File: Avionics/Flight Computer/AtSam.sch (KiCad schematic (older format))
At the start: 0 parts

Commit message: Restarted initial layout and cleaned up decoupling/RF layout.
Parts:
- added U12: ATSAME70Q21A-AN, Housings_QFP:LQFP-144_20x20mm_Pitch0.5mm, symbol ATSAME70Q21A-AN
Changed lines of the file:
@@
 EESchema Schematic File Version 2
+LIBS:Flight Computer-rescue
 LIBS:device
 LIBS:rfcom
@@
 $Descr A4 11693 8268
 encoding utf-8
-Sheet 2 7
+Sheet 2 9
 Title ""
 Date ""
@@
 Comment4 ""
 $EndDescr
+$Comp
+L ATSAME70Q21A-AN U12
+U 1 1 58B40577
+P 3150 1900
+F 0 "U12" H 3150 3067 50  0000 C CNN
+F 1 "ATSAME70Q21A-AN" H 3150 2976 50  0000 C CNN
+F 2 "Housings_QFP:LQFP-144_20x20mm_Pitch0.5mm" H 800 4750 50  0001 C CIN
+F 3 "http://www.atmel.com/Images/Atmel-11296-32-bit-Cortex-M7-Microcontroller-SAM-E70Q-SAM-E70N-SAM-E70J_Datasheet.pdf" H 800 -4300 50  0001 C CNN
+	1    3150 1900
+	1    0    0    -1
+$EndComp
+$Comp
+L ATSAME70Q21A-AN U12
+U 2 1 58B4060F
+P 3150 4050
+F 0 "U12" H 3150 5067 50  0000 C CNN
+F 1 "ATSAME70Q21A-AN" H 3150 4976 50  0000 C CNN
+F 2 "Housings_QFP:LQFP-144_20x20mm_Pitch0.5mm" H -100 3900 50  0001 C CIN
+F 3 "http://www.atmel.com/Images/Atmel-11296-32-bit-Cortex-M7-Microcontroller-SAM-E70Q-SAM-E70N-SAM-E70J_Datasheet.pdf" H -100 -5150 50  0001 C CNN
+	2    3150 4050
+	1    0    0    -1
+$EndComp
+$Comp
+L ATSAME70Q21A-AN U12
+U 3 1 58B4068D
+P 2900 5950
+F 0 "U12" H 2800 6750 50  0000 L CNN
+F 1 "ATSAME70Q21A-AN" H 2500 6650 50  0000 L CNN
+F 2 "Housings_QFP:LQFP-144_20x20mm_Pitch0.5mm" H -4500 8350 50  0001 C CIN
+F 3 "http://www.atmel.com/Images/Atmel-11296-32-bit-Cortex-M7-Microcontroller-SAM-E70Q-SAM-E70N-SAM-E70J_Datasheet.pdf" H -4500 -700 50  0001 C CNN
+	3    2900 5950
+	1    0    0    -1
+$EndComp
+$Comp
+L ATSAME70Q21A-AN U12
+U 4 1 58B406DD
+P 7250 1750
+F 0 "U12" H 7250 2767 50  0000 C CNN
+F 1 "ATSAME70Q21A-AN" H 7250 2676 50  0000 C CNN
+F 2 "Housings_QFP:LQFP-144_20x20mm_Pitch0.5mm" H -50 2100 50  0001 C CIN
+F 3 "http://www.atmel.com/Images/Atmel-11296-32-bit-Cortex-M7-Microcontroller-SAM-E70Q-SAM-E70N-SAM-E70J_Datasheet.pdf" H -50 -6950 50  0001 C CNN
+	4    7250 1750
+	1    0    0    -1
+$EndComp
+$Comp
+L ATSAME70Q21A-AN U12
+U 5 1 58B4072D
+P 7250 3850
+F 0 "U12" H 7250 4867 50  0000 C CNN
+F 1 "ATSAME70Q21A-AN" H 7250 4776 50  0000 C CNN
+F 2 "Housings_QFP:LQFP-144_20x20mm_Pitch0.5mm" H -2400 6150 50  0001 C CIN
+F 3 "http://www.atmel.com/Images/Atmel-11296-32-bit-Cortex-M7-Microcontroller-SAM-E70Q-SAM-E70N-SAM-E70J_Datasheet.pdf" H -2400 -2900 50  0001 C CNN
+	5    7250 3850
+	1    0    0    -1
+$EndComp
+$Comp
+L ATSAME70Q21A-AN U12
+U 6 1 58B407D7
+P 7000 5450
+F 0 "U12" H 6900 5950 50  0000 L CNN
+F 1 "ATSAME70Q21A-AN" H 6600 5850 50  0000 L CNN
+F 2 "Housings_QFP:LQFP-144_20x20mm_Pitch0.5mm" H -2500 5250 50  0001 C CIN
+F 3 "http://www.atmel.com/Images/Atmel-11296-32-bit-Cortex-M7-Microcontroller-SAM-E70Q-SAM-E70N-SAM-E70J_Datasheet.pdf" H -2500 -3800 50  0001 C CNN
+	6    7000 5450
+	1    0    0    -1
+$EndComp
 $EndSCHEMATC

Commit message: Nearly completed initial placement.
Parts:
- added C57, C69, C72, C73, C74, C75, C76, C77, C78, C79, C80, C81, C82, C83, C84: 0.1u, Capacitors_SMD:C_0402, symbol C
- added C60, C62, C63, C64, C65: 12p, Capacitors_SMD:C_0402, symbol C
- added C61, C68: 1u, Capacitors_SMD:C_0603, symbol C
- added C85, C86: 4.7u, Capacitors_SMD:C_0603, symbol C
- added L19, L20: MMZ1005Y471CTD25, Inductors_SMD:L_0402, symbol L
- added L21: LQM21FN100M70L, Inductors_SMD:L_0805, symbol L
- added R20: 5.62k, Resistors_SMD:R_0402, symbol R
- added R21: 22k, Resistors_SMD:R_0402, symbol R
- added R22: 15k, Resistors_SMD:R_0402, symbol R
- added R23: 2.2, Resistors_SMD:R_0402, symbol R
- added Y1: 9HT11-32.768KDZB-T, Crystals:Crystal_SMD_2012-2pin_2.0x1.2mm, symbol Crystal
- added Y2: 7V-16.000MAHJ-T, Crystals:Crystal_SMD_3225-4pin_3.2x2.5mm, symbol Crystal_GND24
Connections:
- net labels added: +3.3V, GND, QCS, QIO0, QIO1, QIO2, QIO3, QIO[0..3], QSCK, USBD_N, USBD_P, VBUS_DETECT, VDDPLLUSB, VUSB
- wire segments 0 -> 70
- no-connect marks 0 -> 2
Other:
- note added: "Pin 5"
- note added: "Place one near each VDDCORE pin"
- note added: "Place one near each VDDIO pin"
- moved on the sheet: U12A, U12B, U12C, U12D, U12E, U12F

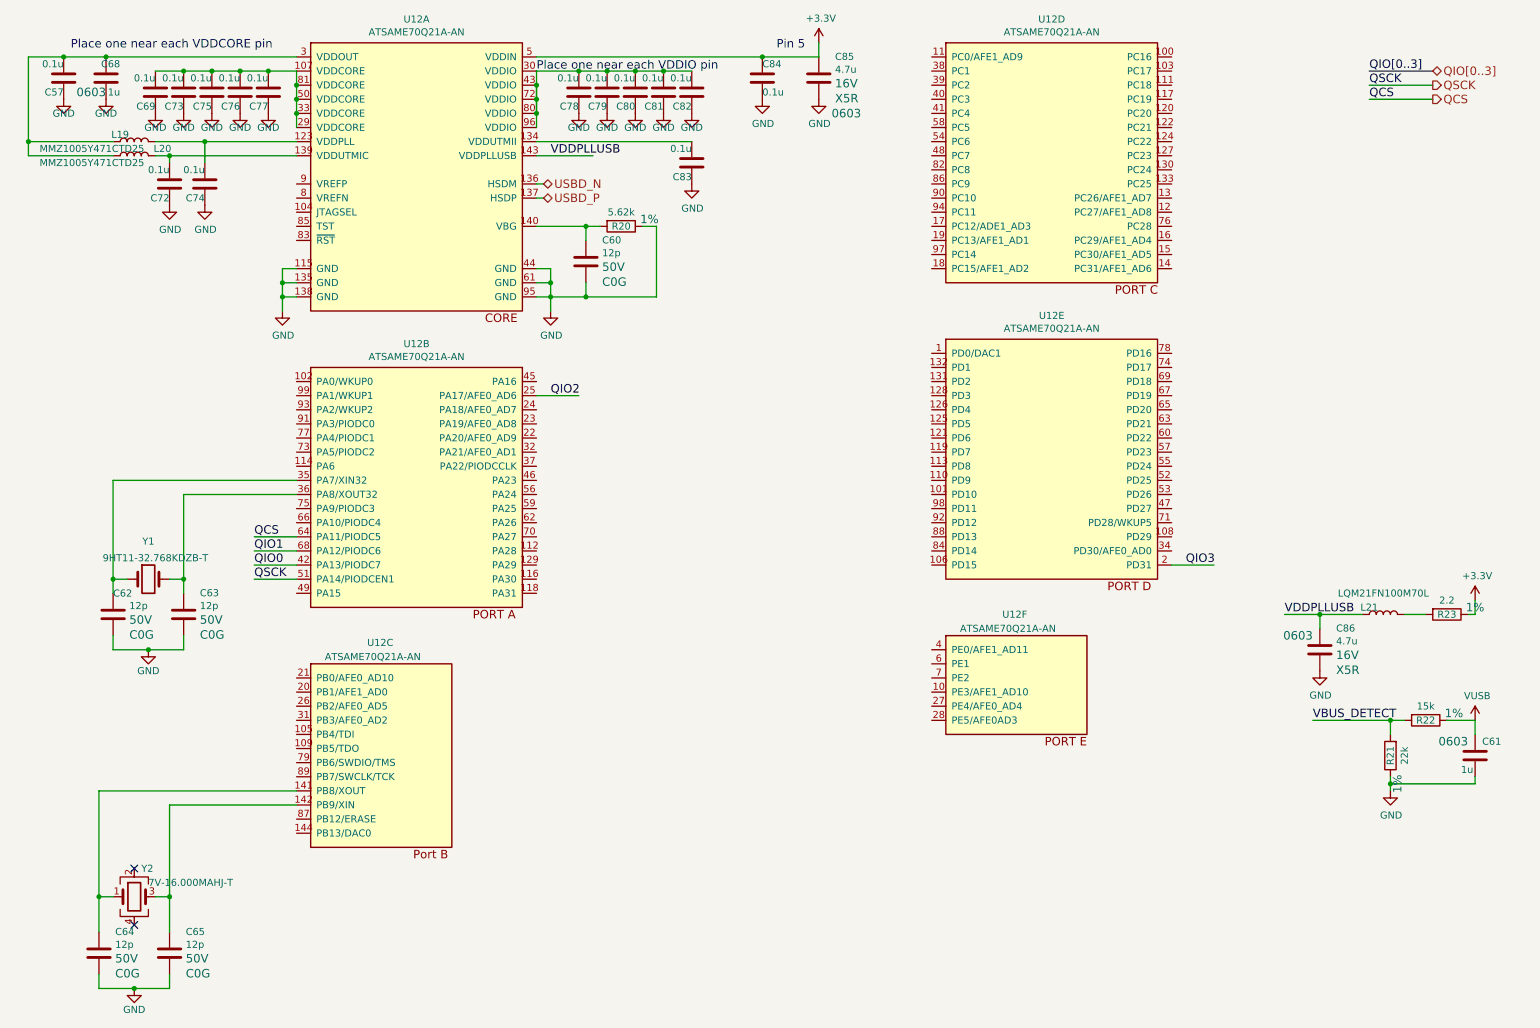
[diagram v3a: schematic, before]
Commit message: Added additional pinout
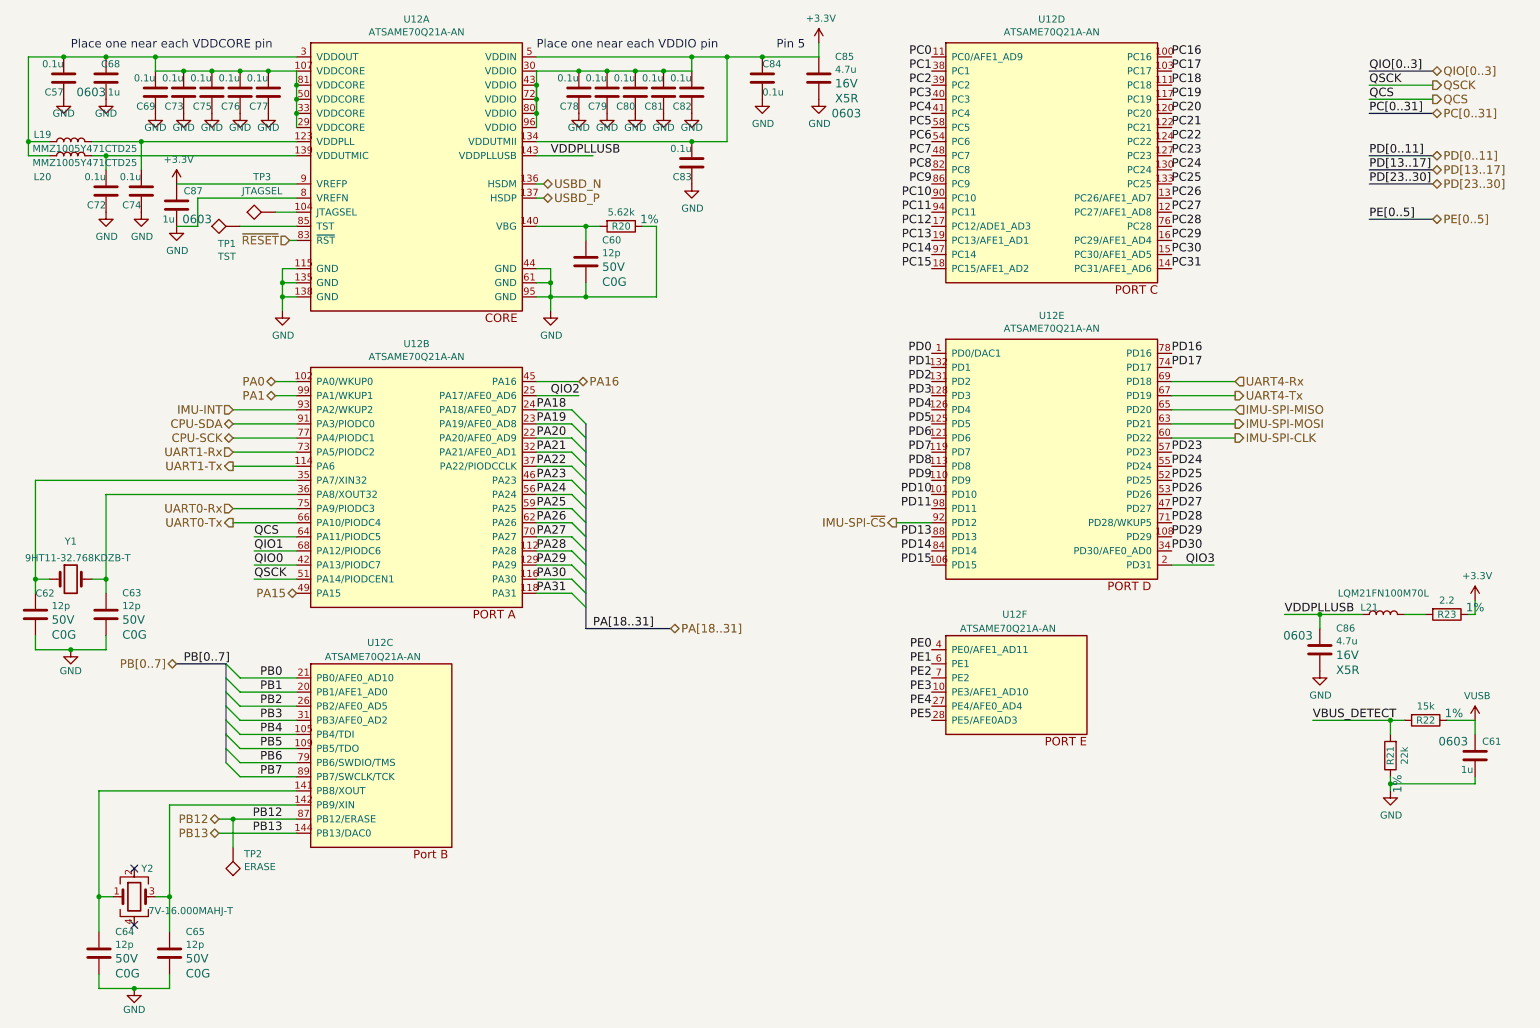
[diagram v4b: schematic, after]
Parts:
- added C87: 1u, Capacitors_SMD:C_0603, symbol C
- added TP1: TST, Measurement_Points:Measurement_Point_Round-SMD-Pad_Small, symbol TEST
- added TP2: ERASE, Measurement_Points:Measurement_Point_Round-SMD-Pad_Small, symbol TEST
- added TP3: JTAGSEL, Measurement_Points:Measurement_Point_Round-SMD-Pad_Small, symbol TEST
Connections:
- net labels added: CPU-SCK, CPU-SDA, IMU-INT, IMU-SPI-CLK, IMU-SPI-MISO, IMU-SPI-MOSI, IMU-SPI-~CS, PA0, PA1, PA15, PA16, PA18, PA19, PA20, PA21, PA22, PA23, PA24, PA25, PA26, PA27, PA28, PA29, PA30, PA31, PA[18..31], PB0, PB1, PB12, PB13, PB2, PB3, PB4, PB5, PB6, PB7, PB[0..7], PC0, PC1, PC10, PC11, PC12, PC13, PC14, PC15, PC16, PC17, PC18, PC19, PC2, PC20, PC21, PC22, PC23, PC24, PC25, PC26, PC27, PC28, PC29, PC3, PC30, PC31, PC4, PC5, PC6, PC7, PC8, PC9, PC[0..31], PD0, PD1, PD10, PD11, PD13, PD14, PD15, PD16, PD17, PD2, PD23, PD24, PD25, PD26, PD27, PD28, PD29, PD3, PD30, PD4, PD5, PD6, PD7, PD8, PD9, PD[0..11], PD[13..17], PD[23..30], PE0, PE1, PE2, PE3, PE4, PE5, PE[0..5], UART0-Rx, UART0-Tx, UART1-Rx, UART1-Tx, UART4-Rx, UART4-Tx, ~RESET
- wire segments 70 -> 121
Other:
- moved on the sheet: C62, C63, C72, C74, L19, L20, Y1

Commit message: Wired up everything and started rearranging layout
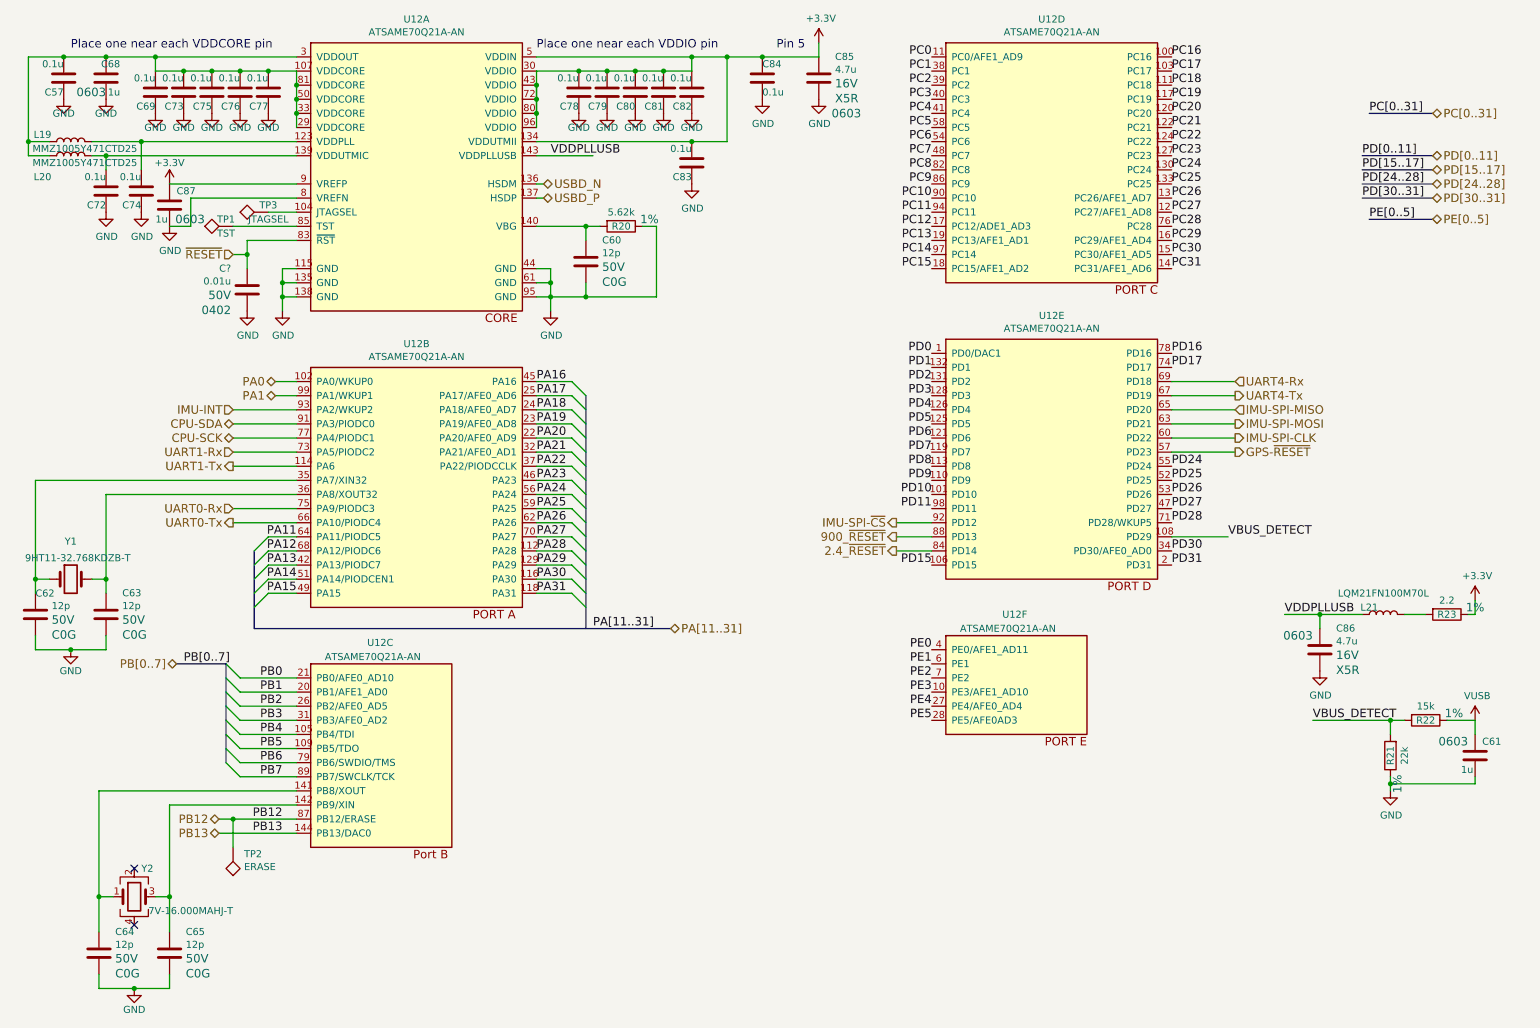
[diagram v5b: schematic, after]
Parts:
- added C?: 0.01u, Capacitors_SMD:C_0402, symbol C
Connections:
- net PD29 is gone; now on net VBUS_DETECT: U12.108 (PD29)
- net GND: now also C?.2
- net ~RESET: now also C?.1
- net PD13 renamed 900_~RESET
- net PD14 renamed 2.4_~RESET
- net PD23 renamed GPS-~RESET
- net QCS renamed PA11
- net QIO0 renamed PA13
- net QIO1 renamed PA12
- net QIO2 renamed PA17
- net QIO3 renamed PD31
- net QSCK renamed PA14
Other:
- moved on the sheet: C87, TP1, TP3

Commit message: Finished breaking out signals to connector sheet and interconnecting processors.
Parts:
- gave numbers to parts that had none: 1
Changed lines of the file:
@@
 $EndComp
 $Comp
-L +3.3V #PWR01
+L +3.3V #PWR03
 U 1 1 58B891F6
 P 6200 900
-F 0 "#PWR01" H 4500 -1600 50  0001 C CNN
+F 0 "#PWR03" H 4500 -1600 50  0001 C CNN
 F 1 "+3.3V" H 6215 1073 50  0000 C CNN
 F 2 "" H 4500 -1450 50  0001 C CNN
@@
 $EndComp
 $Comp
-L GND #PWR02
+L GND #PWR04
 U 1 1 58B89232
 P 2400 2800
-F 0 "#PWR02" H 1100 750 50  0001 C CNN
+F 0 "#PWR04" H 1100 750 50  0001 C CNN
 F 1 "GND" H 2405 2627 50  0000 C CNN
 F 2 "" H 1100 1000 50  0001 C CNN
@@
 $EndComp
 $Comp
-L GND #PWR03
+L GND #PWR05
 U 1 1 58B892B4
 P 4300 2800
-F 0 "#PWR03" H 3000 750 50  0001 C CNN
+F 0 "#PWR05" H 3000 750 50  0001 C CNN
 F 1 "GND" H 4305 2627 50  0000 C CNN
 F 2 "" H 3000 1000 50  0001 C CNN
@@
 $EndComp
 $Comp
-L GND #PWR04
+L GND #PWR06
 U 1 1 58B8B12B
 P 10250 6200
-F 0 "#PWR04" H 8950 4150 50  0001 C CNN
+F 0 "#PWR06" H 8950 4150 50  0001 C CNN
 F 1 "GND" H 10255 6027 50  0000 C CNN
 F 2 "" H 8950 4400 50  0001 C CNN
@@
 VBUS_DETECT
 $Comp
-L VUSB #PWR05
+L VUSB #PWR07
 U 1 1 58B8B57E
 P 10850 5700
-F 0 "#PWR05" H 10900 5750 50  0001 C CNN
+F 0 "#PWR07" H 10900 5750 50  0001 C CNN
 F 1 "VUSB" H 10865 5873 50  0000 C CNN
 F 2 "" H 150 450 50  0001 C CNN
@@
 	650  5200 650  5100
 $Comp
-L GND #PWR06
+L GND #PWR08
 U 1 1 58B9AEC4
 P 900 5200
-F 0 "#PWR06" H 900 4950 50  0001 C CNN
+F 0 "#PWR08" H 900 4950 50  0001 C CNN
 F 1 "GND" H 900 5050 50  0000 C CNN
 F 2 "" H 900 5200 50  0001 C CNN
@@
 	1100 7600 1100 7500
 $Comp
-L GND #PWR07
+L GND #PWR09
 U 1 1 58BA68B9
 P 1350 7600
-F 0 "#PWR07" H 1350 7350 50  0001 C CNN
+F 0 "#PWR09" H 1350 7350 50  0001 C CNN
 F 1 "GND" H 1350 7450 50  0000 C CNN
 F 2 "" H 1350 7600 50  0001 C CNN
@@
 Connection ~ 5800 1000
 $Comp
-L GND #PWR08
+L GND #PWR010
 U 1 1 58B7BFAA
 P 5800 1300
-F 0 "#PWR08" H 4500 -750 50  0001 C CNN
+F 0 "#PWR010" H 4500 -750 50  0001 C CNN
 F 1 "GND" H 5805 1127 50  0000 C CNN
 F 2 "" H 4500 -500 50  0001 C CNN
@@
 $EndComp
 $Comp
-L GND #PWR09
+L GND #PWR011
 U 1 1 58B7C131
 P 6200 1300
-F 0 "#PWR09" H 4900 -750 50  0001 C CNN
+F 0 "#PWR011" H 4900 -750 50  0001 C CNN
 F 1 "GND" H 6205 1127 50  0000 C CNN
 F 2 "" H 4900 -500 50  0001 C CNN
@@
 $EndComp
 $Comp
-L GND #PWR010
+L GND #PWR012
 U 1 1 58B7D83B
 P 5300 1400
-F 0 "#PWR010" H 4000 -650 50  0001 C CNN
+F 0 "#PWR012" H 4000 -650 50  0001 C CNN
 F 1 "GND" H 5300 1300 50  0000 C CNN
 F 2 "" H 4000 -400 50  0001 C CNN
@@
 $EndComp
 $Comp
-L GND #PWR011
+L GND #PWR013
 U 1 1 58B7D876
 P 5100 1400
-F 0 "#PWR011" H 3800 -650 50  0001 C CNN
+F 0 "#PWR013" H 3800 -650 50  0001 C CNN
 F 1 "GND" H 5100 1300 50  0000 C CNN
 F 2 "" H 3800 -400 50  0001 C CNN
@@
 $EndComp
 $Comp
-L GND #PWR012
+L GND #PWR014
 U 1 1 58B7D8B1
 P 4900 1400
-F 0 "#PWR012" H 3600 -650 50  0001 C CNN
+F 0 "#PWR014" H 3600 -650 50  0001 C CNN
 F 1 "GND" H 4900 1300 50  0000 C CNN
 F 2 "" H 3600 -400 50  0001 C CNN
@@
 $EndComp
 $Comp
-L GND #PWR013
+L GND #PWR015
 U 1 1 58B7D8EC
 P 4700 1400
-F 0 "#PWR013" H 3400 -650 50  0001 C CNN
+F 0 "#PWR015" H 3400 -650 50  0001 C CNN
 F 1 "GND" H 4700 1300 50  0000 C CNN
 F 2 "" H 3400 -400 50  0001 C CNN
@@
 $EndComp
 $Comp
-L GND #PWR014
+L GND #PWR016
 U 1 1 58B7D927
 P 4500 1400
-F 0 "#PWR014" H 3200 -650 50  0001 C CNN
+F 0 "#PWR016" H 3200 -650 50  0001 C CNN
 F 1 "GND" H 4500 1300 50  0000 C CNN
 F 2 "" H 3200 -400 50  0001 C CNN
@@
 Connection ~ 1400 1600
 $Comp
-L GND #PWR015
+L GND #PWR017
 U 1 1 58B82BC8
 P 1150 2100
-F 0 "#PWR015" H -150 50  50  0001 C CNN
+F 0 "#PWR017" H -150 50  50  0001 C CNN
 F 1 "GND" H 1155 1927 50  0000 C CNN
 F 2 "" H -150 300 50  0001 C CNN
@@
 $EndComp
 $Comp
-L GND #PWR016
+L GND #PWR018
 U 1 1 58B82D5B
 P 1400 2100
-F 0 "#PWR016" H 100 50  50  0001 C CNN
+F 0 "#PWR018" H 100 50  50  0001 C CNN
 F 1 "GND" H 1405 1927 50  0000 C CNN
 F 2 "" H 100 300 50  0001 C CNN
@@
 $EndComp
 $Comp
-L GND #PWR017
+L GND #PWR019
 U 1 1 58B8358A
 P 2300 1400
-F 0 "#PWR017" H 1000 -650 50  0001 C CNN
+F 0 "#PWR019" H 1000 -650 50  0001 C CNN
 F 1 "GND" H 2300 1300 50  0000 C CNN
 F 2 "" H 1000 -400 50  0001 C CNN
@@
 $EndComp
 $Comp
-L GND #PWR018
+L GND #PWR020
 U 1 1 58B83590
 P 2100 1400
-F 0 "#PWR018" H 800 -650 50  0001 C CNN
+F 0 "#PWR020" H 800 -650 50  0001 C CNN
 F 1 "GND" H 2100 1300 50  0000 C CNN
 F 2 "" H 800 -400 50  0001 C CNN
@@
 $EndComp
 $Comp
-L GND #PWR019
+L GND #PWR021
 U 1 1 58B83596
 P 1900 1400
-F 0 "#PWR019" H 600 -650 50  0001 C CNN
+F 0 "#PWR021" H 600 -650 50  0001 C CNN
 F 1 "GND" H 1900 1300 50  0000 C CNN
 F 2 "" H 600 -400 50  0001 C CNN
@@
 $EndComp
 $Comp
-L GND #PWR020
+L GND #PWR022
 U 1 1 58B8359C
 P 1700 1400
-F 0 "#PWR020" H 400 -650 50  0001 C CNN
+F 0 "#PWR022" H 400 -650 50  0001 C CNN
 F 1 "GND" H 1700 1300 50  0000 C CNN
 F 2 "" H 400 -400 50  0001 C CNN
@@
 $EndComp
 $Comp
-L GND #PWR021
+L GND #PWR023
 U 1 1 58B835A2
 P 1500 1400
-F 0 "#PWR021" H 200 -650 50  0001 C CNN
+F 0 "#PWR023" H 200 -650 50  0001 C CNN
 F 1 "GND" H 1500 1300 50  0000 C CNN
 F 2 "" H 200 -400 50  0001 C CNN
@@
 $EndComp
 $Comp
-L GND #PWR022
+L GND #PWR024
 U 1 1 58B86F94
 P 1150 1300
-F 0 "#PWR022" H -150 -750 50  0001 C CNN
+F 0 "#PWR024" H -150 -750 50  0001 C CNN
 F 1 "GND" H 1150 1200 50  0000 C CNN
 F 2 "" H -150 -500 50  0001 C CNN
@@
 $EndComp
 $Comp
-L GND #PWR023
+L GND #PWR025
 U 1 1 58B86FE5
 P 850 1300
-F 0 "#PWR023" H -450 -750 50  0001 C CNN
+F 0 "#PWR025" H -450 -750 50  0001 C CNN
 F 1 "GND" H 850 1200 50  0000 C CNN
 F 2 "" H -450 -500 50  0001 C CNN
@@
 $EndComp
 $Comp
-L GND #PWR024
+L GND #PWR026
 U 1 1 58B8A103
 P 5300 1900
-F 0 "#PWR024" H 4000 -150 50  0001 C CNN
+F 0 "#PWR026" H 4000 -150 50  0001 C CNN
 F 1 "GND" H 5305 1727 50  0000 C CNN
 F 2 "" H 4000 100 50  0001 C CNN
@@
 VDDPLLUSB
 $Comp
-L +3.3V #PWR025
+L +3.3V #PWR027
 U 1 1 58B8D10C
 P 10850 4850
-F 0 "#PWR025" H 9150 2350 50  0001 C CNN
+F 0 "#PWR027" H 9150 2350 50  0001 C CNN
 F 1 "+3.3V" H 10865 5023 50  0000 C CNN
 F 2 "" H 9150 2500 50  0001 C CNN
@@
 	9500 4950 10050 4950
 $Comp
-L GND #PWR026
+L GND #PWR028
 U 1 1 58B8E11D
 P 9750 5350
-F 0 "#PWR026" H 8450 3300 50  0001 C CNN
+F 0 "#PWR028" H 8450 3300 50  0001 C CNN
 F 1 "GND" H 9755 5177 50  0000 C CNN
 F 2 "" H 8450 3550 50  0001 C CNN
@@
 	1750 2200 1600 2200
 $Comp
-L +3.3V #PWR027
+L +3.3V #PWR029
 U 1 1 58B9C26A
 P 1600 1900
-F 0 "#PWR027" H -100 -600 50  0001 C CNN
+F 0 "#PWR029" H -100 -600 50  0001 C CNN
 F 1 "+3.3V" H 1600 2050 50  0000 C CNN
 F 2 "" H -100 -450 50  0001 C CNN
@@
 $EndComp
 $Comp
-L GND #PWR028
+L GND #PWR030
 U 1 1 58B9C685
 P 1600 2200
-F 0 "#PWR028" H 300 150 50  0001 C CNN
+F 0 "#PWR030" H 300 150 50  0001 C CNN
 F 1 "GND" H 1605 2027 50  0000 C CNN
 F 2 "" H 300 400 50  0001 C CNN
@@
 PD31
 $Comp
-L C C?
+L C C59
 U 1 1 58C25D8A
 P 2150 2650
-F 0 "C?" H 2036 2802 50  0000 R CNN
+F 0 "C59" H 2036 2802 50  0000 R CNN
 F 1 "0.01u" H 2036 2711 50  0000 R CNN
 F 2 "Capacitors_SMD:C_0402" H -3562 -200 50  0001 C CNN
@@
 $EndComp
 $Comp
-L GND #PWR?
+L GND #PWR031
 U 1 1 58C25D91
 P 2150 2800
-F 0 "#PWR?" H 2200 2850 50  0001 C CNN
+F 0 "#PWR031" H 2200 2850 50  0001 C CNN
 F 1 "GND" H 2155 2627 50  0000 C CNN
 F 2 "" H -4650 -950 50  0001 C CNN
